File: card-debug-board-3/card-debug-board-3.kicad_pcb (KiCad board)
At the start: 4 copper layers, 54 x 64 mm, 94 parts, among them J1 USB4105-GF-A, J2 USB4105-GF-A, J3 Conn_01x05, J4 5040501291, J5 2-1734592-0, Q1 PMV450ENEAR, SW1 B3F-1000, SW2 PCM13SMTR, SW3 B3F-1000, SW4 78RB02T, U1 MIC5205-3.3YM5, U2 W25Q16JVSS, U3 RP2040, U4 74AUP1G17, U5 74AUP1G17, U6 IP4234CZ6,125, U7 IP4234CZ6,125, Y1 12 MHz

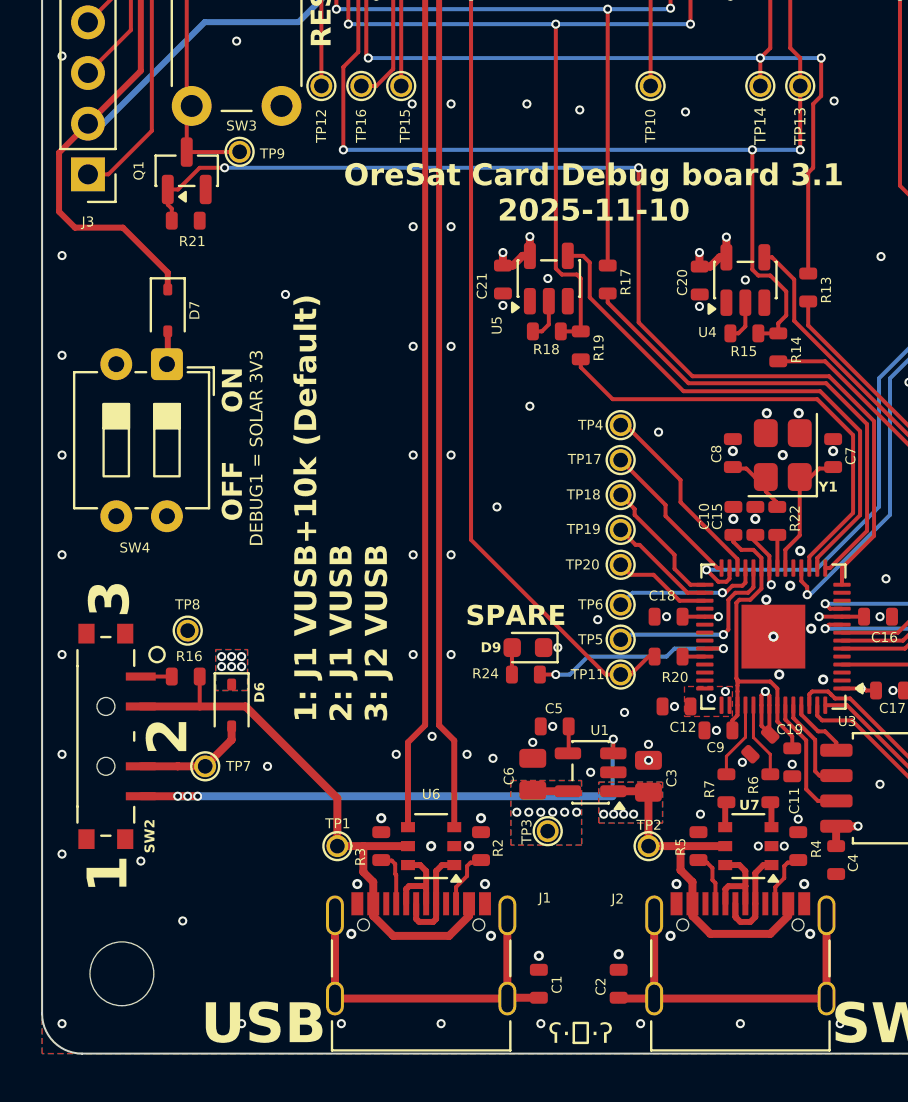
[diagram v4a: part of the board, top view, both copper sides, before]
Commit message: Fix labeling of the 3.0 power slide switch which was exactly backwards.
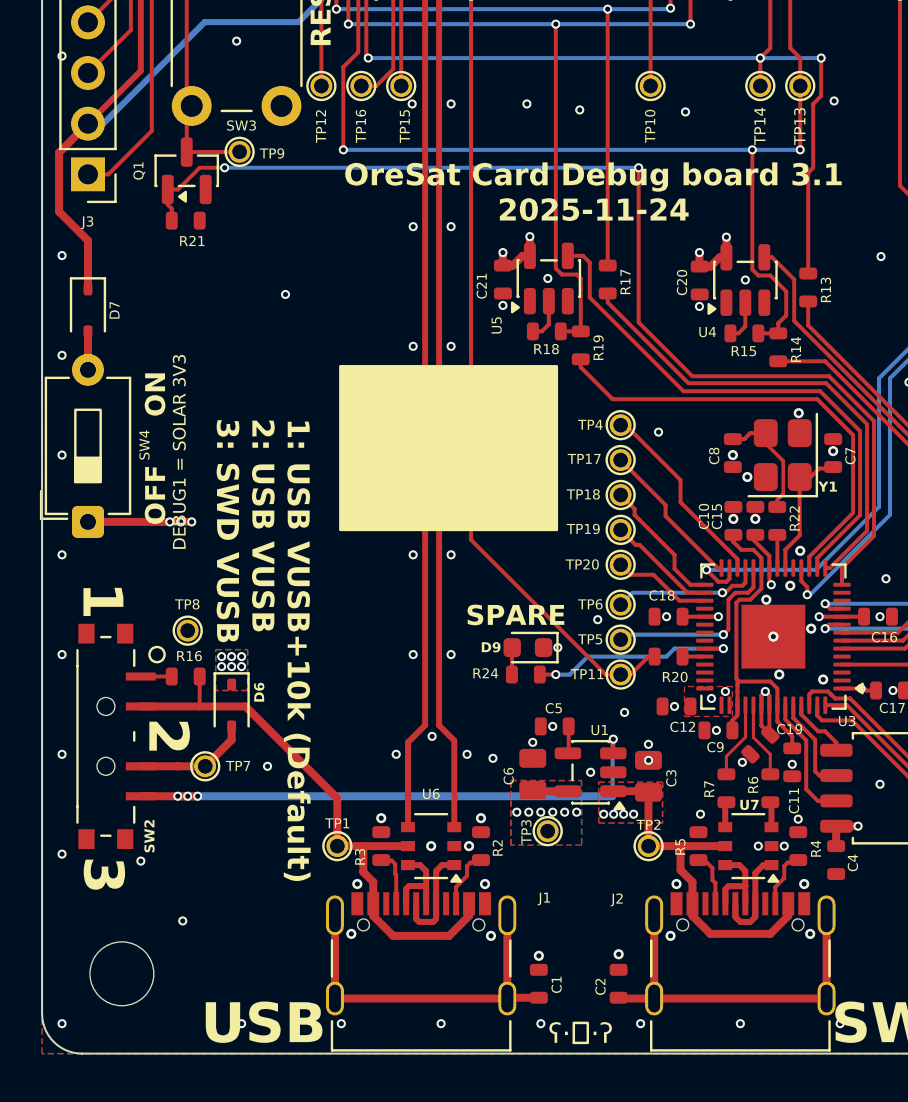
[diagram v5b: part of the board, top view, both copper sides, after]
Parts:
- R2, R3, R4, R5: value 10k -> 5.1k
- SW4: value 78RB02T -> SW_DIP_x01; footprint Button_Switch_THT:SW_DIP_SPSTx02_Slide_6.7x6.64mm_W7.62mm_P2.54mm_LowProfile -> Button_Switch_THT:SW_DIP_SPSTx01_Slide_6.7x4.1mm_W7.62mm_P2.54mm_LowProfile
- moved SW4 8.84 mm to (148.3, 83.3), turned to 90 degrees
- moved D7 4.00 mm to (148.3, 72.8)
- turned C8 to 90 degrees
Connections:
- SW4 pad 1: Net-(D7-A) -> +3.3V
- SW4 pad 2: unconnected-(SW4-Pad2) -> Net-(D7-A)
- Y1 pad 3: GND -> Net-(C8-Pad2)
- Y1 pad 4: Net-(C8-Pad2) -> GND
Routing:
- net +3.3V: track 23.7 -> 28.9 mm, vias 18 -> 21
- net /DBG1/SM3V3: track 71.7 -> 68.6 mm
- net Net-(C8-Pad2): track 4.21 -> 5.96 mm
- net GND: vias 153 -> 152
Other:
- board text added: "1: USB VUSB+10k (Default) 2: USB VUSB 3: SWD VUSB"
- board text removed: "1: J1 VUSB+10k (Default) 2: J1 VUSB 3: J2 VUSB"

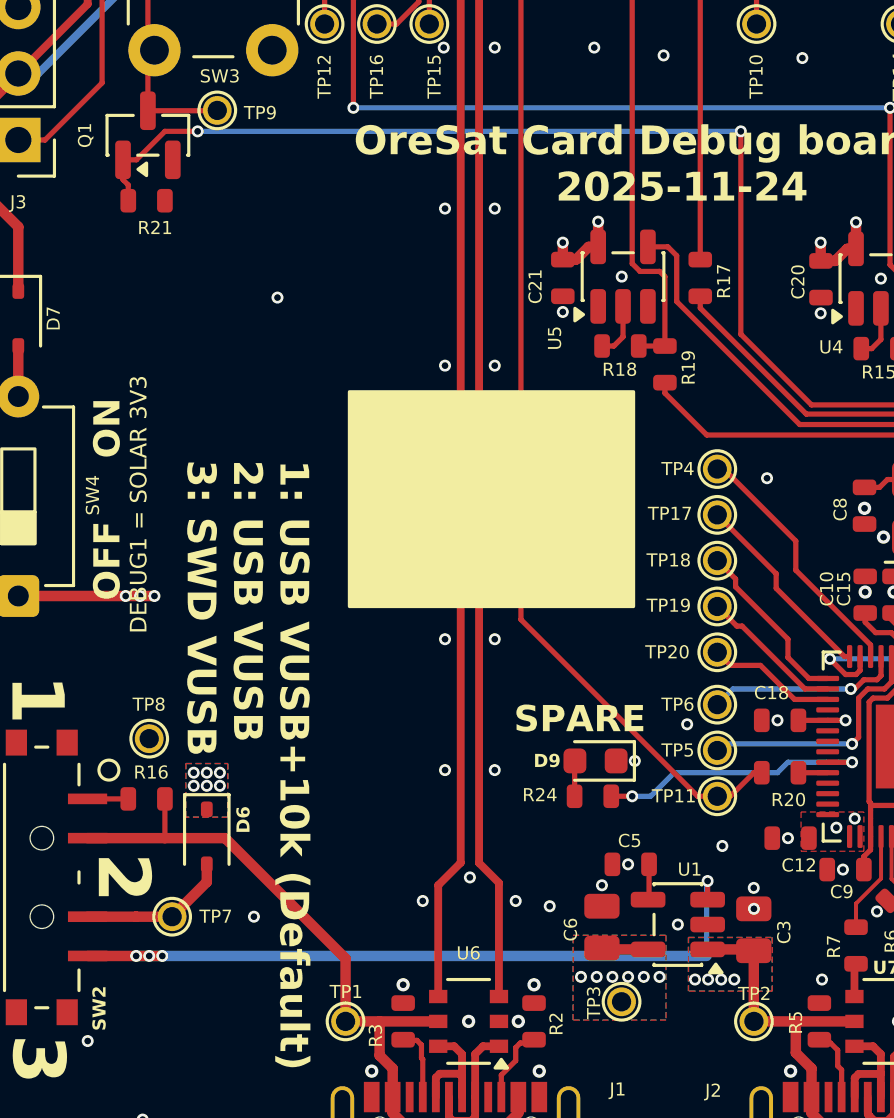
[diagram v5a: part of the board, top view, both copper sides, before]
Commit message: Cleanup and last features.
Added ability for the RP2040 to power the DUT using a GPIO line. Cleaned up ERC and DRC. Updated symbols and footprints.
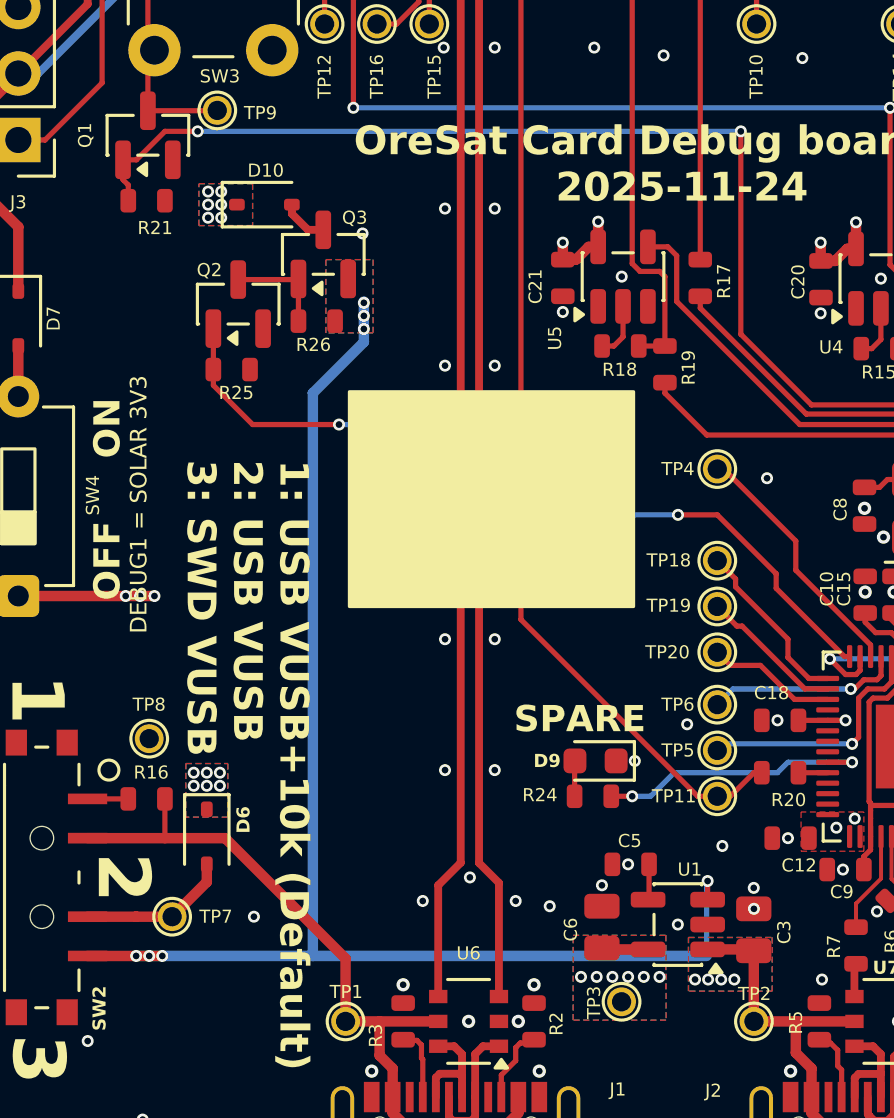
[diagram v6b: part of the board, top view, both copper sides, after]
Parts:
- removed TP17: TestPoint-MinTH, oresat-misc:TestPoint-MinTH
- added D10: ZLLS410TA, Diode_SMD:D_SOD-323, F.Cu at (157.7, 68.4)
- added Q2: PMV450ENEAR, Package_TO_SOT_SMD:SOT-23, F.Cu at (156.7, 72.2)
- added Q3: NTR4101P, Package_TO_SOT_SMD:SOT-23, F.Cu at (159.9, 70.3)
- added R25: 10k, oresat-passives:0603-C-NOSILK, F.Cu at (156.4, 74.7)
- added R26: 10k, oresat-passives:0603-C-NOSILK, F.Cu at (159.7, 72.8)
- R21: value 1k -> 10k
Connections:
- net /RESET_TARGET renamed /TARGET_RESET
- U3 pad 28: Net-(U3-GPIO17) -> /TARGET_POWER
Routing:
- net /TARGET_POWER: track 0.00 -> 31.1 mm, vias 0 -> 2
- net VBUS2: track 46.8 -> 72.6 mm, vias 8 -> 11
- net Net-(U3-GPIO17): track 7.62 -> 0.00 mm
- net Net-(Q2-D): track 0.00 -> 3.92 mm
- net Net-(D10-A): track 0.00 -> 1.80 mm
- net /VBUSP: vias 16 -> 22

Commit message: BOM cleanup; fabbing v3.1git add .
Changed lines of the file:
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@@
 	(title_block
 		(title "Card Debug Board")
-		(date "2025-11-24")
+		(date "2026-02-08")
 		(rev "3.1")
 		(company "Portland State Aerosapce Society")

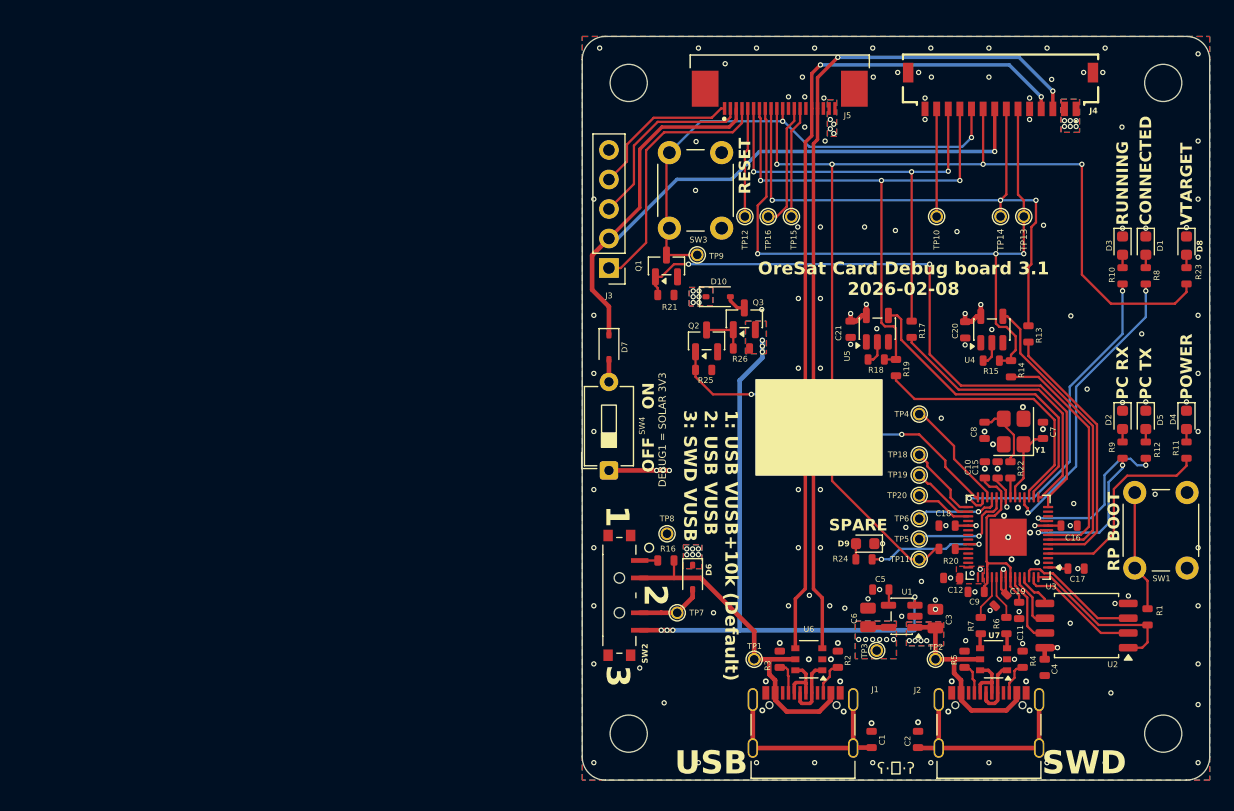
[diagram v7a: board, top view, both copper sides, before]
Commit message: Card Debug Board v3.2
Fixed SW2 through-holes which have never been right, added fiducials, added makefile and readmes.
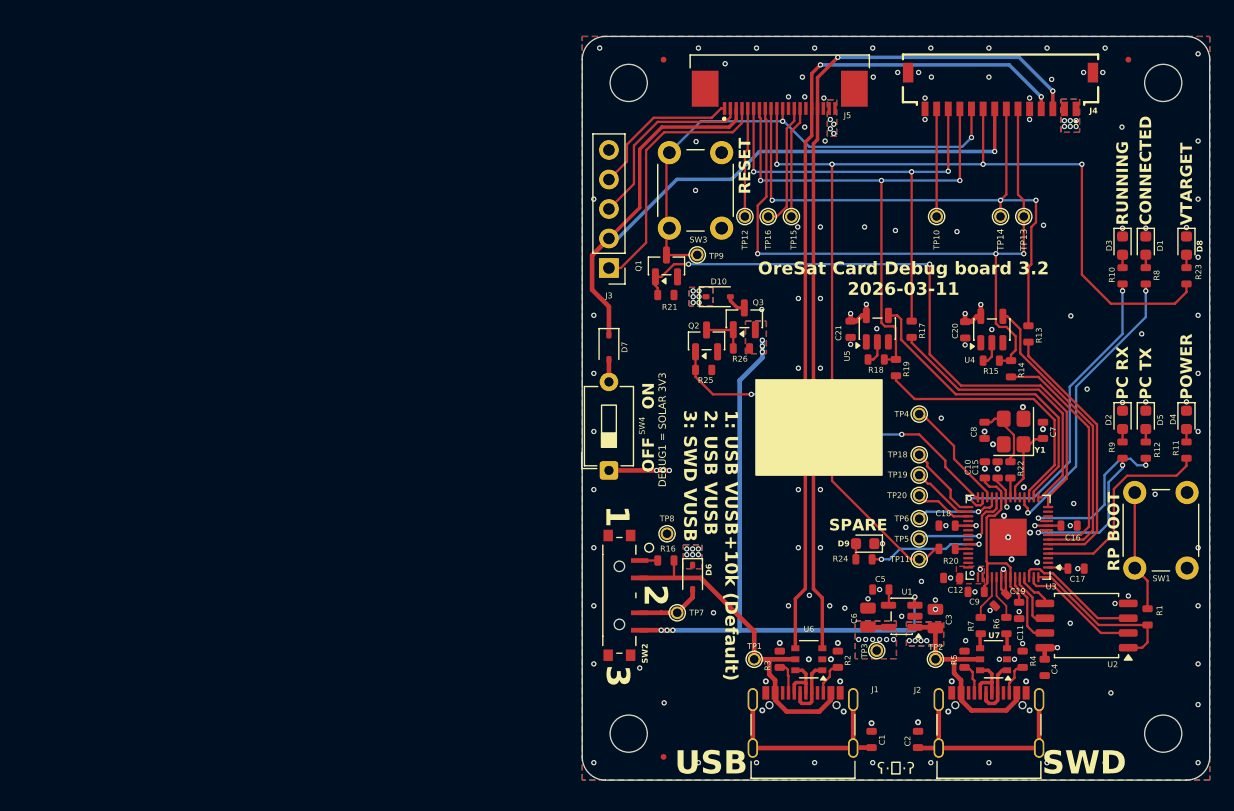
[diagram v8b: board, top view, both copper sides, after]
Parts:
- added FID101: Fiducial, Fiducial:Fiducial_0.5mm_Mask1mm, F.Cu at (153.0, 48.0)
- added FID102: Fiducial, Fiducial:Fiducial_0.5mm_Mask1mm, F.Cu at (193.0, 48.0)
- added FID103: Fiducial, Fiducial:Fiducial_0.5mm_Mask1mm, F.Cu at (153.0, 108.0)
